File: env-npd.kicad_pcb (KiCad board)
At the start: 2 copper layers, 105.4 x 96 mm, 39 parts

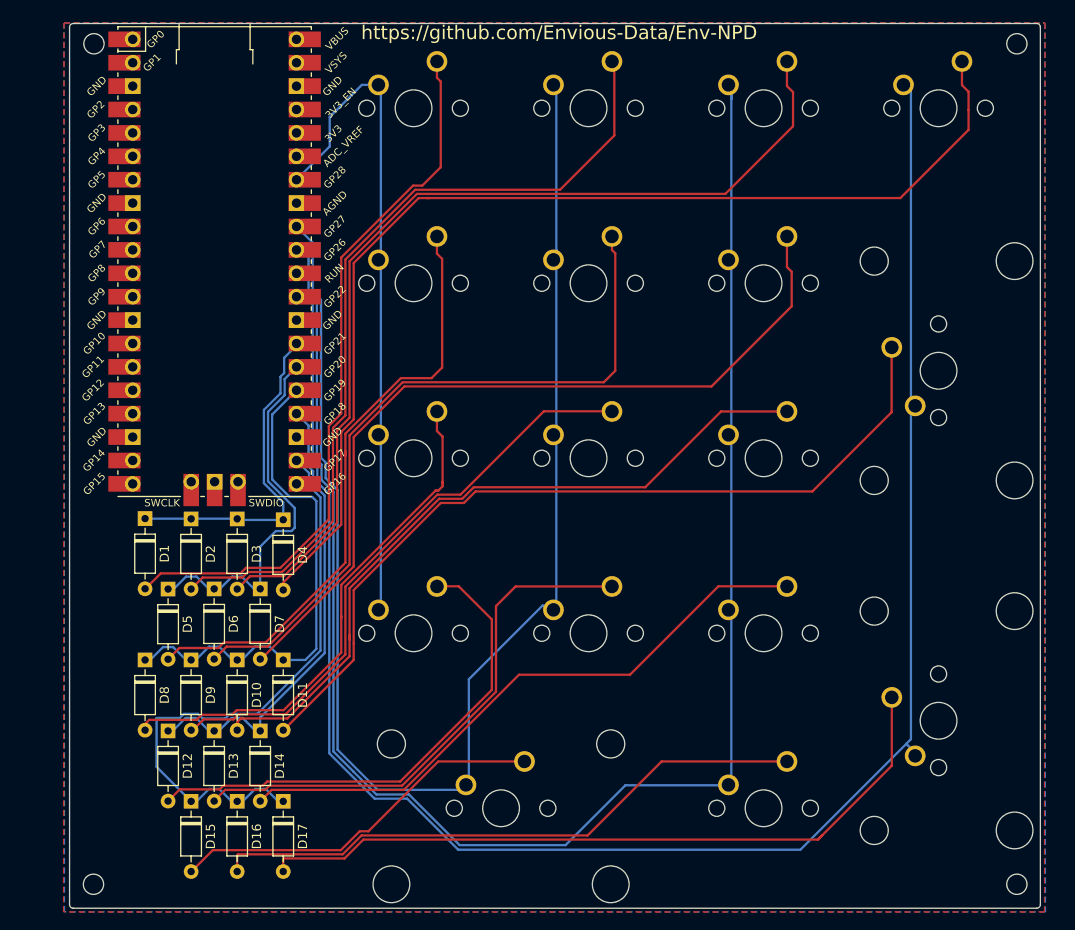
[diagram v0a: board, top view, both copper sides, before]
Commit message: I couldn't sleep so I re-designed the pcb a bit and may actually order some for my self (since I need me a numpad)
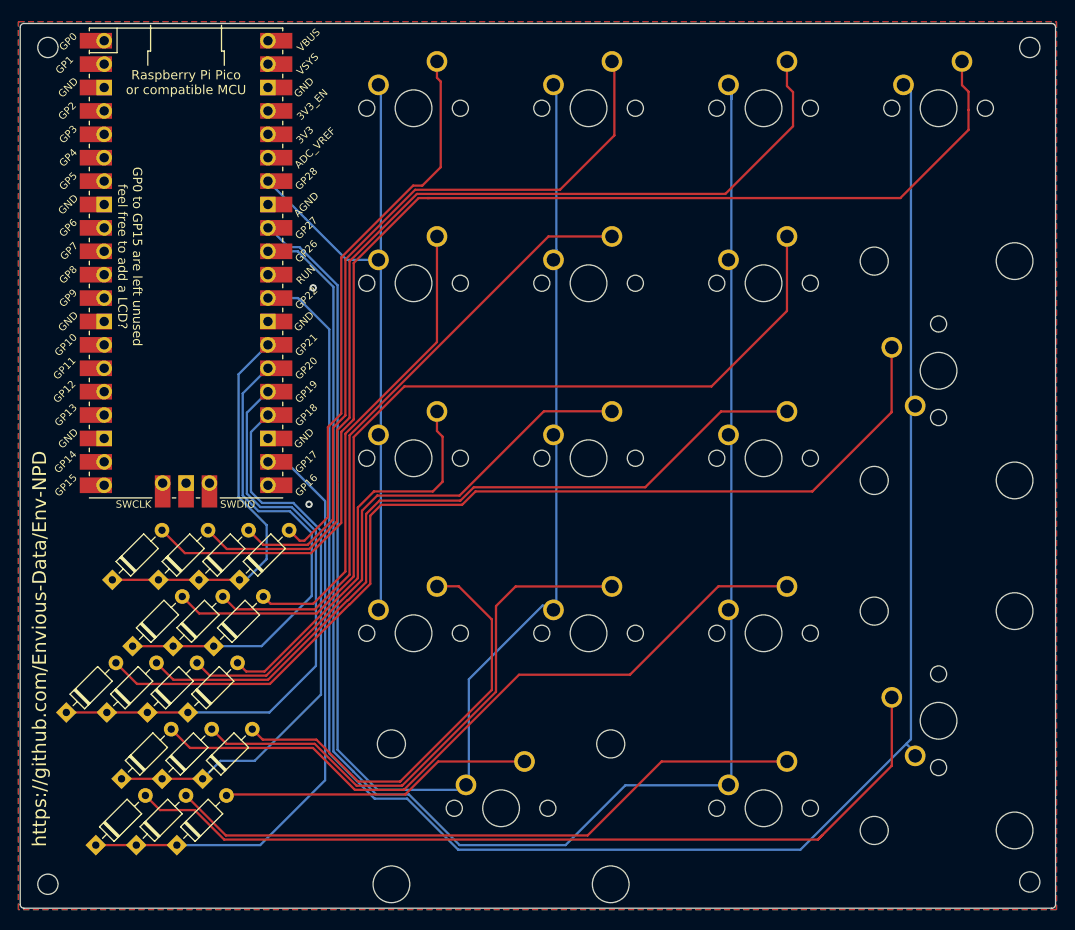
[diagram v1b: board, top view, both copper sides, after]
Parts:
- moved D11 24.2 mm to (72.8, 133.6), turned to 45 degrees
- moved D17 20.9 mm to (76.0, 148.0), turned to 45 degrees
- moved D4 19.7 mm to (77.8, 119.2), turned to 45 degrees
- moved D14 15.9 mm to (78.8, 140.8), turned to 45 degrees
- moved D10 15.3 mm to (77.2, 133.6), turned to 45 degrees
- moved D7 15.2 mm to (80.0, 126.4), turned to 45 degrees
- moved D1 12.2 mm to (91.6, 119.2), turned to 45 degrees
- moved D16 11.9 mm to (80.4, 148.0), turned to 45 degrees
- moved D3 10.8 mm to (82.8, 119.2), turned to 45 degrees
- moved D5 7.93 mm to (88.8, 126.4), turned to 45 degrees
- moved D13 7.68 mm to (83.2, 140.8), turned to 45 degrees
- moved D6 7.65 mm to (84.4, 126.4), turned to 45 degrees
- moved D9 7.42 mm to (81.6, 133.6), turned to 45 degrees
- moved D8 7.36 mm to (86.0, 133.6), turned to 45 degrees
- moved D2 6.67 mm to (87.2, 119.2), turned to 45 degrees
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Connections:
- MCU1 pad 33: Net-(MCU1-Pad33) -> GND
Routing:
- net Net-(D1-Pad2): track 78.6 -> 61.0 mm
- net Net-(D11-Pad2): track 91.8 -> 108.7 mm
- net Net-(D5-Pad2): track 66.0 -> 51.2 mm
- net Net-(D17-Pad2): track 79.7 -> 94.4 mm
- net Net-(D8-Pad2): track 56.8 -> 43.6 mm
- net Net-(D14-Pad2): track 67.0 -> 78.8 mm
- net Net-(D4-Pad2): track 119.6 -> 131.3 mm
- net row1: track 41.4 -> 52.7 mm
- net Net-(D6-Pad2): track 79.5 -> 68.5 mm
- net row3: track 51.3 -> 61.7 mm
- net row2: track 55.3 -> 65.0 mm
- net Net-(D2-Pad2): track 90.3 -> 82.7 mm
- net Net-(D12-Pad2): track 55.0 -> 47.4 mm
- net Net-(D7-Pad2): track 89.6 -> 97.0 mm
- net Net-(D15-Pad2): track 41.2 -> 33.9 mm
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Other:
- board size 105.4 x 96 mm -> 112.4 x 96 mm
- board text added: "GP0 to GP15 are left unused feel free to add a LCD?"
- board text added: "Raspberry Pi Pico or compatible MCU"
- board text added: "Tohster"
